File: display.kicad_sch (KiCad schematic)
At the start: 53 parts, among them Q3 SSM6N35AFE, Q4 SSM6N35AFE

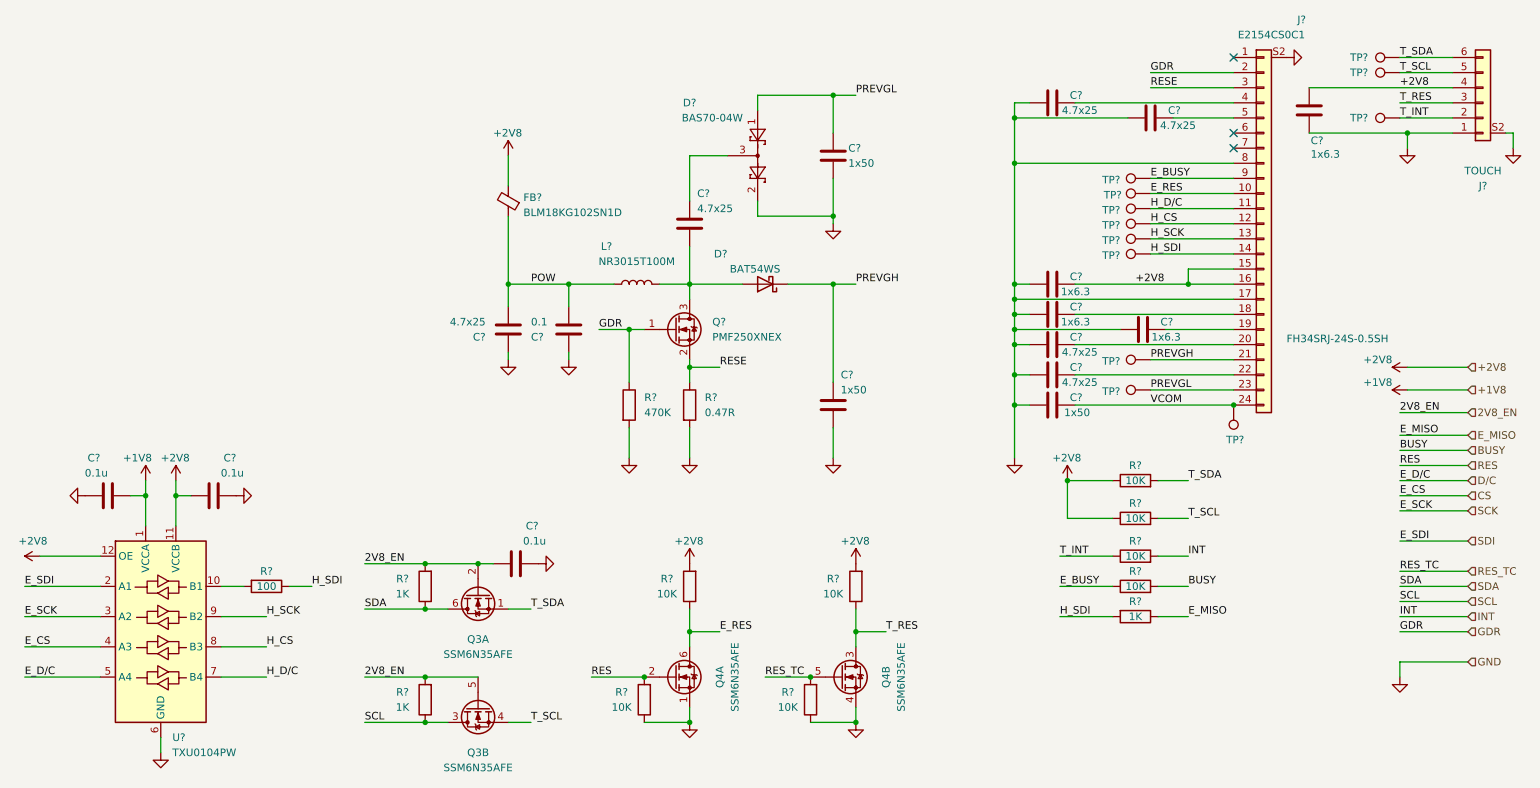
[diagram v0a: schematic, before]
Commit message: Fix capacitor values
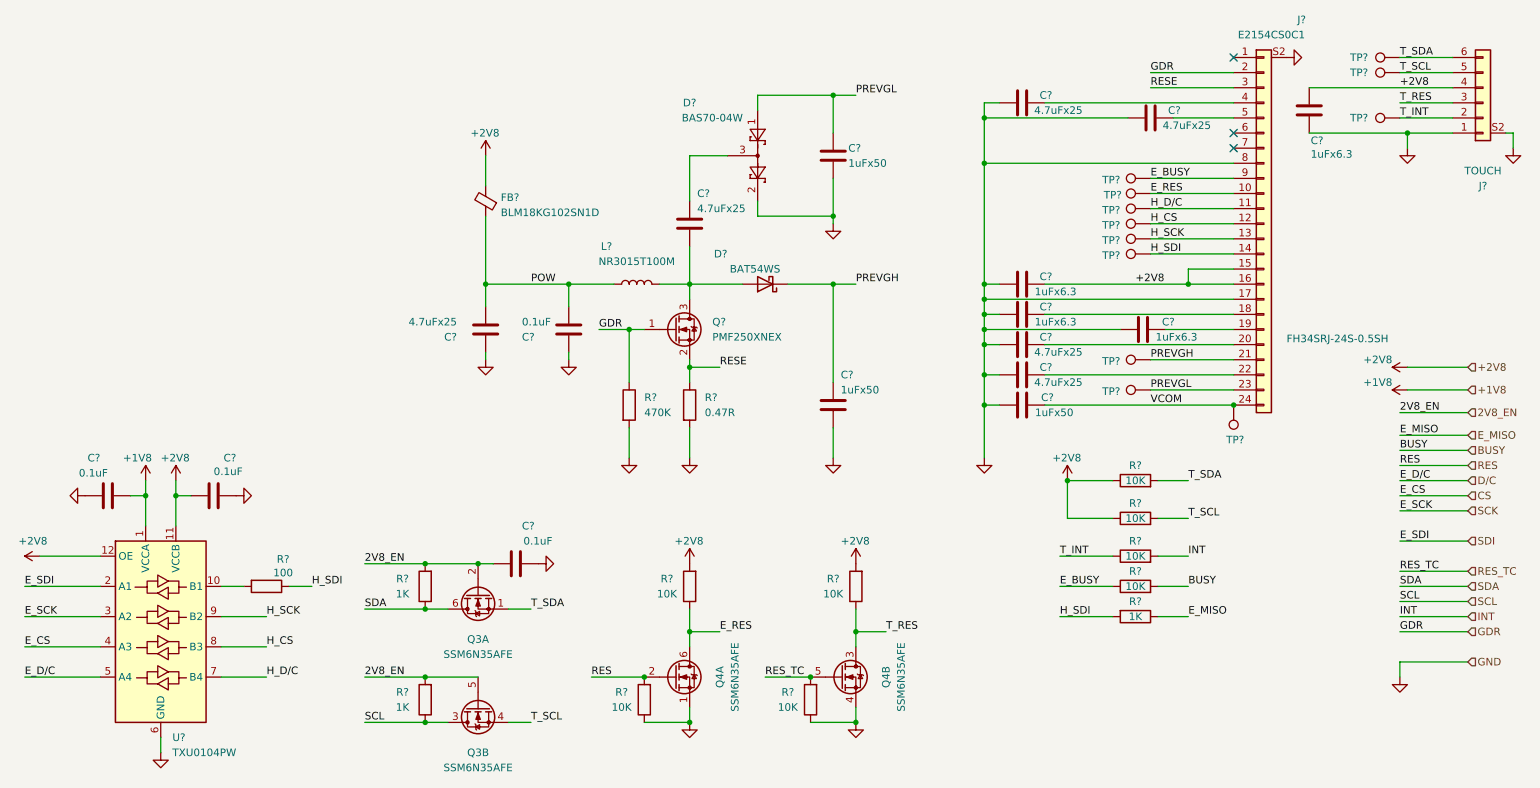
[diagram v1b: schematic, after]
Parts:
- C? (x4): value 1x6.3 -> 1uFx6.3
- C? (x6): value 4.7x25 -> 4.7uFx25
- C? (x3): value 1x50 -> 1uFx50
- C?: value 0.1 -> 0.1uF
- C? (x3): value 0.1u -> 0.1uF
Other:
- moved on the sheet: C?, FB?

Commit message: Fill up mouser part numbers
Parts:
- C? (x4): MouserPN (none) -> 963-JMK105BJ105KV-F
- C? (x6): MouserPN (none) -> 581-02013A100J
- C? (x3): MouserPN (none) -> 81-GRM155R61H105ME5J
- C? (x4): MouserPN (none) -> 581-KGM05AR71C104KN
- D?: MouserPN (none) -> 621-BAT54WS-F
- D?: MouserPN (none) -> 726-BAS7004WH6327
- FB?: MouserPN (none) -> 81-BLM18KG102SN1D
- L?: MouserPN (none) -> 963-NR3015T100M
- Q?: MouserPN (none) -> 771-PMF250XNEX
- U?: MouserPN (none) -> 595-TXU0104PWR

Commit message: Finish BOM components filling
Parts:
- J?: MouserPN (none) -> 798-FH34SRJ24S05SH50
- J?: MouserPN (none) -> 798-FH34SRJ6S05SH50
- Q3, Q4: MouserPN (none) -> 757-SSM6N35AFELF
- R? (x8): MouserPN (none) -> 71-CRCW040210K0FKEDC
- R? (x3): MouserPN (none) -> 603-RC0402FR-071KL
- R?: MouserPN (none) -> 603-RC0402FR-7D470KL
- R?: MouserPN (none) -> 594-MCS04020C1000FE0
- R?: MouserPN (none) -> 588-KDV06DR470ET
- TP? (x12): now left out of the parts list
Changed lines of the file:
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@@
 			)
 		)
-		(property "MouserPN" ""
+		(property "MouserPN" "71-CRCW040210K0FKEDC"
 			(at 128.27 137.16 0)
 			(effects
@@
 			)
 		)
-		(property "MouserPN" ""
+		(property "MouserPN" "71-CRCW040210K0FKEDC"
 			(at 135.89 118.11 0)
 			(effects
@@
 			)
 		)
-		(property "MouserPN" ""
+		(property "MouserPN" "603-RC0402FR-071KL"
 			(at 91.44 118.11 0)
 			(effects
@@
 			)
 		)
-		(property "MouserPN" ""
+		(property "MouserPN" "71-CRCW040210K0FKEDC"
 			(at 210.82 106.68 0)
 			(effects
@@
 		(unit 1)
 		(exclude_from_sim no)
-		(in_bom yes)
+		(in_bom no)
 		(on_board yes)
 		(dnp no)
@@
 		(unit 1)
 		(exclude_from_sim no)
-		(in_bom yes)
+		(in_bom no)
 		(on_board yes)
 		(dnp no)
@@
 			)
 		)
-		(property "MouserPN" ""
+		(property "MouserPN" "603-RC0402FR-071KL"
 			(at 91.44 137.16 0)
 			(effects
@@
 		(unit 1)
 		(exclude_from_sim no)
-		(in_bom yes)
+		(in_bom no)
 		(on_board yes)
 		(dnp no)
@@
 		(unit 1)
 		(exclude_from_sim no)
-		(in_bom yes)
+		(in_bom no)
 		(on_board yes)
 		(dnp no)
@@
 			)
 		)
-		(property "MouserPN" ""
+		(property "MouserPN" "71-CRCW040210K0FKEDC"
 			(at 156.21 137.16 0)
 			(effects
@@
 			)
 		)
-		(property "MouserPN" ""
+		(property "MouserPN" "71-CRCW040210K0FKEDC"
 			(at 210.82 118.11 0)
 			(effects
@@
 		(unit 1)
 		(exclude_from_sim no)
-		(in_bom yes)
+		(in_bom no)
 		(on_board yes)
 		(dnp no)
@@
 			)
 		)
-		(property "MouserPN" ""
+		(property "MouserPN" "71-CRCW040210K0FKEDC"
 			(at 210.82 100.33 0)
 			(effects
@@
 			)
 		)
-		(property "MouserPN" ""
+		(property "MouserPN" "603-RC0402FR-7D470KL"
 			(at 125.73 87.63 0)
 			(effects
@@
 		(unit 1)
 		(exclude_from_sim no)
-		(in_bom yes)
+		(in_bom no)
 		(on_board yes)
 		(dnp no)
@@
 			)
 		)
-		(property "MouserPN" ""
+		(property "MouserPN" "798-FH34SRJ24S05SH50"
 			(at 232.41 57.15 0)
 			(effects
@@
 		(unit 1)
 		(exclude_from_sim no)
-		(in_bom yes)
+		(in_bom no)
 		(on_board yes)
 		(dnp no)
@@
 			)
 		)
-		(property "MouserPN" ""
+		(property "MouserPN" "594-MCS04020C1000FE0"
 			(at 64.77 118.11 0)
 			(effects
@@
 			)
 		)
-		(property "MouserPN" ""
+		(property "MouserPN" "757-SSM6N35AFELF"
 			(at 133.35 133.35 0)
 			(effects
@@
 			)
 		)
-		(property "MouserPN" ""
+		(property "MouserPN" "71-CRCW040210K0FKEDC"
 			(at 163.83 118.11 0)
 			(effects
@@
 			)
 		)
-		(property "MouserPN" ""
+		(property "MouserPN" "71-CRCW040210K0FKEDC"
 			(at 210.82 113.03 0)
 			(effects
@@
 			)
 		)
-		(property "MouserPN" ""
+		(property "MouserPN" "757-SSM6N35AFELF"
 			(at 161.29 133.35 0)
 			(effects
@@
 			)
 		)
-		(property "MouserPN" ""
+		(property "MouserPN" "757-SSM6N35AFELF"
 			(at 100.33 138.43 0)
 			(effects
@@
 			)
 		)
-		(property "MouserPN" ""
+		(property "MouserPN" "798-FH34SRJ6S05SH50"
 			(at 269.24 36.83 0)
 			(effects
@@
 		(unit 1)
 		(exclude_from_sim no)
-		(in_bom yes)
+		(in_bom no)
 		(on_board yes)
 		(dnp no)
@@
 			)
 		)
-		(property "MouserPN" ""
+		(property "MouserPN" "757-SSM6N35AFELF"
 			(at 100.33 119.38 0)
 			(effects
@@
 		(unit 1)
 		(exclude_from_sim no)
-		(in_bom yes)
+		(in_bom no)
 		(on_board yes)
 		(dnp no)
@@
 			)
 		)
-		(property "MouserPN" ""
+		(property "MouserPN" "588-KDV06DR470ET"
 			(at 135.89 87.63 0)
 			(effects
@@
 		(unit 1)
 		(exclude_from_sim no)
-		(in_bom yes)
+		(in_bom no)
 		(on_board yes)
 		(dnp no)
@@
 		(unit 1)
 		(exclude_from_sim no)
-		(in_bom yes)
+		(in_bom no)
 		(on_board yes)
 		(dnp no)
@@
 			)
 		)
-		(property "MouserPN" ""
+		(property "MouserPN" "603-RC0402FR-071KL"
 			(at 210.82 123.19 0)
 			(effects
@@
 		(unit 1)
 		(exclude_from_sim no)
-		(in_bom yes)
+		(in_bom no)
 		(on_board yes)
 		(dnp no)

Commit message: Fix BOM
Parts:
- C? (x6): MouserPN 581-02013A100J -> 581-06033D475KAT2A
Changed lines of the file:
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@@
 			)
 		)
-		(property "MouserPN" "581-02013A100J"
+		(property "MouserPN" "581-06033D475KAT2A"
 			(at 191.77 82.55 0)
 			(effects
@@
 			)
 		)
-		(property "MouserPN" "581-02013A100J"
+		(property "MouserPN" "581-06033D475KAT2A"
 			(at 135.89 57.15 0)
 			(effects
@@
 			)
 		)
-		(property "MouserPN" "581-02013A100J"
+		(property "MouserPN" "581-06033D475KAT2A"
 			(at 191.77 77.47 0)
 			(effects
@@
 			)
 		)
-		(property "MouserPN" "581-02013A100J"
+		(property "MouserPN" "581-06033D475KAT2A"
 			(at 191.77 36.83 0)
 			(effects
@@
 			)
 		)
-		(property "MouserPN" "581-02013A100J"
+		(property "MouserPN" "581-06033D475KAT2A"
 			(at 213.36 39.37 0)
 			(effects
@@
 			)
 		)
-		(property "MouserPN" "581-02013A100J"
+		(property "MouserPN" "581-06033D475KAT2A"
 			(at 101.6 74.93 0)
 			(effects
